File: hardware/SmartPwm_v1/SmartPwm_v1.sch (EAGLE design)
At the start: 41 parts, among them IC1 7805T, J1 ESP32-PICO-KIT, Q1 IRF3704-H, Q2 IRF3704-H, Q3 IRF3704-H, Q4 IRF3704-H, U1 ICL7667CBAZA, U3 ICL7667CBAZA

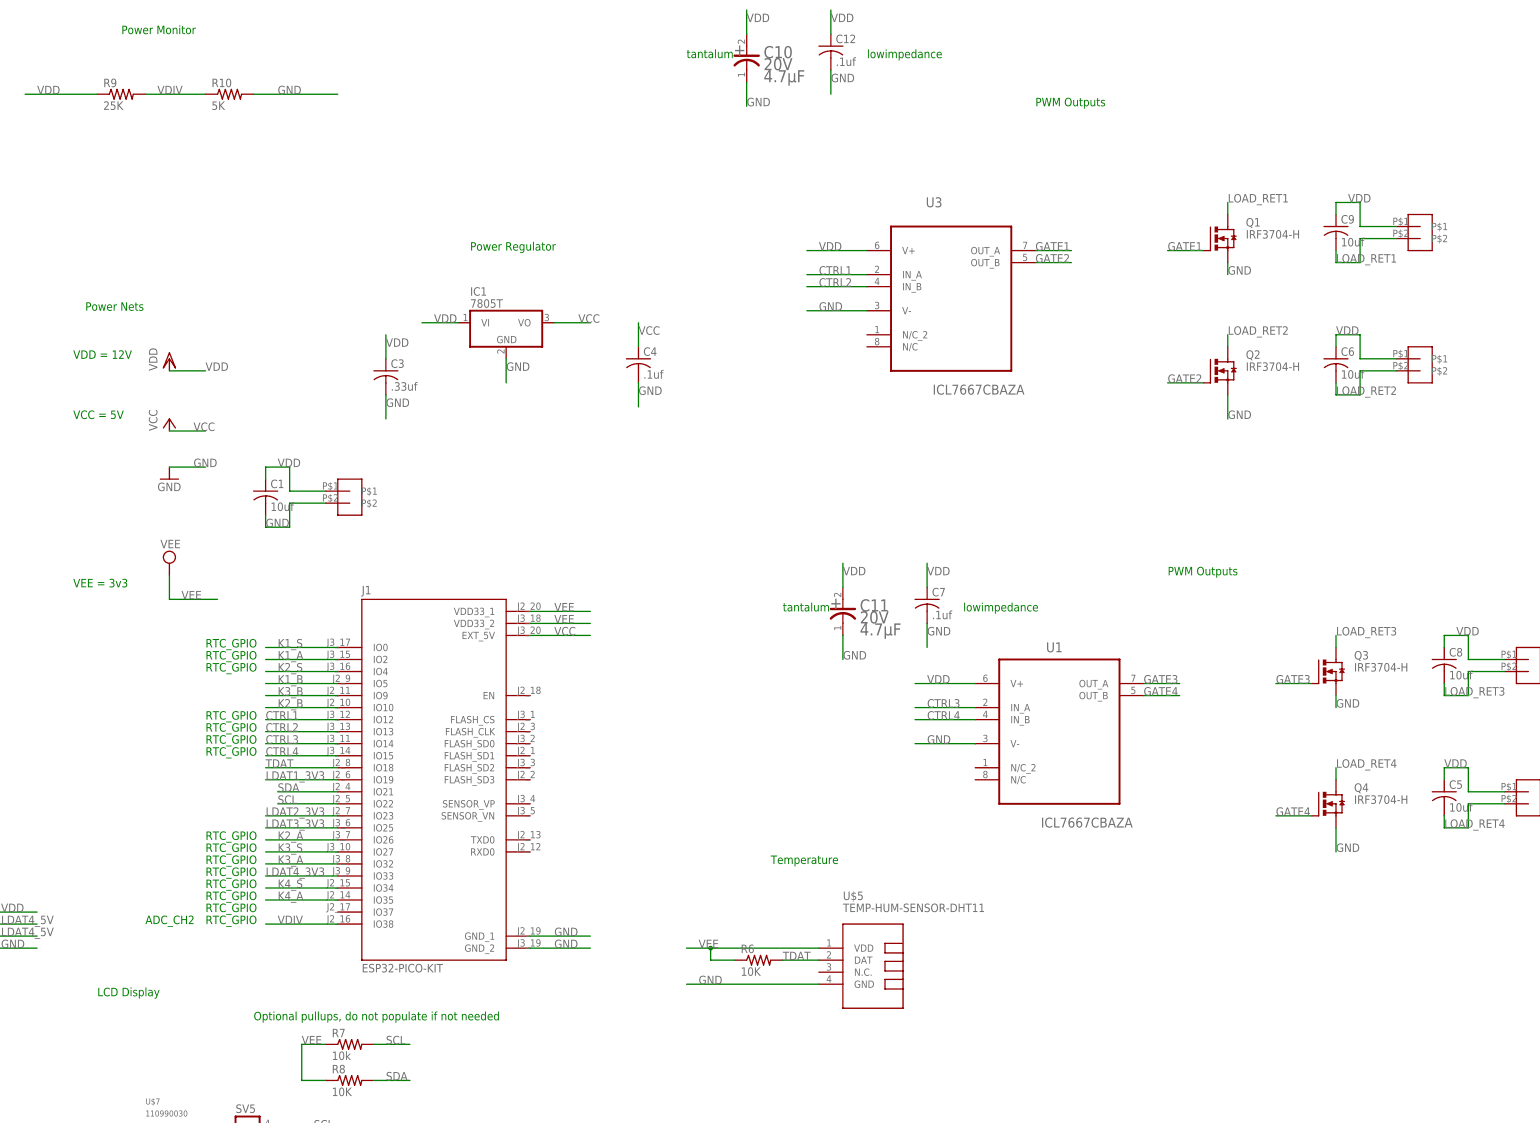
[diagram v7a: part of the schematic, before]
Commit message: redo placment for more efficient routing
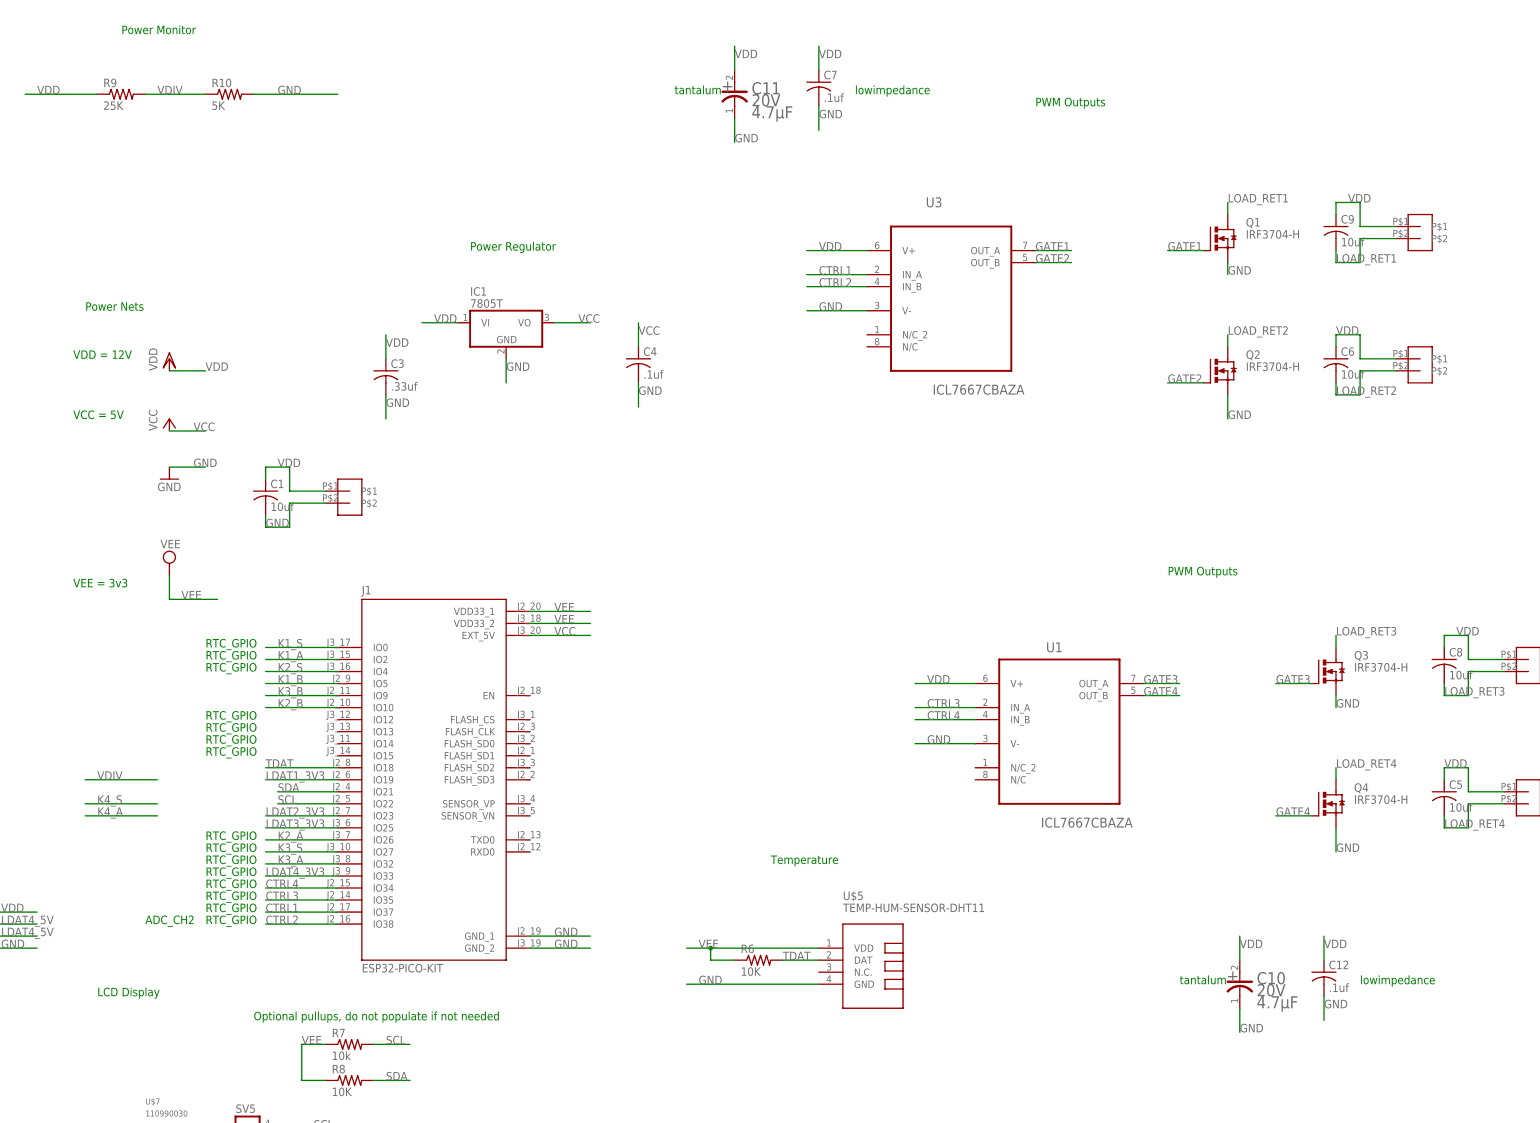
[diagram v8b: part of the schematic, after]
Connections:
- net CTRL1: now also J1.IO37; no longer J1.IO12
- net CTRL2: now also J1.IO38; no longer J1.IO13
- net CTRL3: now also J1.IO35; no longer J1.IO14
- net CTRL4: now also J1.IO34; no longer J1.IO15
- net K4_A: no longer J1.IO35
- net K4_S: no longer J1.IO34
- net VDIV: no longer J1.IO38
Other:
- moved on the sheet: C10, C11, C12, C7
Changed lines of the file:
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@@
 <text x="5.08" y="142.24" size="1.778" layer="91">Power Monitor</text>
 <text x="-5.08" y="25.4" size="1.778" layer="91">VEE = 3v3</text>
-<text x="144.78" y="20.32" size="1.778" layer="91">tantalum</text>
-<text x="182.88" y="20.32" size="1.778" layer="91">lowimpedance</text>
+<text x="121.92" y="129.54" size="1.778" layer="91">tantalum</text>
+<text x="160.02" y="129.54" size="1.778" layer="91">lowimpedance</text>
 <text x="33.02" y="-66.04" size="1.778" layer="91">Optional pullups, do not populate if not needed</text>
 <text x="-15.24" y="-109.22" size="1.778" layer="91">Optional, connector if desired to go grove to grove. beware of orintation during install</text>
-<text x="124.46" y="137.16" size="1.778" layer="91">tantalum</text>
-<text x="162.56" y="137.16" size="1.778" layer="91">lowimpedance</text>
+<text x="228.6" y="-58.42" size="1.778" layer="91">tantalum</text>
+<text x="266.7" y="-58.42" size="1.778" layer="91">lowimpedance</text>
 </plain>
 <instances>
@@
 <attribute name="VALUE" x="10.16" y="-86.36" size="1.27" layer="96"/>
 </instance>
-<instance part="C11" gate="G$0" x="154.94" y="22.86" smashed="yes">
-<attribute name="NAME" x="161.036" y="22.86" size="2.54" layer="95" align="top-left"/>
-</instance>
-<instance part="C7" gate="G$1" x="175.26" y="22.86" smashed="yes">
-<attribute name="NAME" x="176.276" y="23.495" size="1.778" layer="95"/>
-<attribute name="VALUE" x="176.276" y="18.669" size="1.778" layer="96"/>
+<instance part="C11" gate="G$0" x="132.08" y="132.08" smashed="yes">
+<attribute name="NAME" x="138.176" y="132.08" size="2.54" layer="95" align="top-left"/>
+</instance>
+<instance part="C7" gate="G$1" x="152.4" y="132.08" smashed="yes">
+<attribute name="NAME" x="153.416" y="132.715" size="1.778" layer="95"/>
+<attribute name="VALUE" x="153.416" y="127.889" size="1.778" layer="96"/>
 </instance>
 <instance part="C8" gate="G$1" x="284.48" y="10.16" smashed="yes">
@@
 <attribute name="VALUE" x="262.636" y="97.409" size="1.778" layer="96"/>
 </instance>
-<instance part="C10" gate="G$0" x="134.62" y="139.7" smashed="yes">
-<attribute name="NAME" x="140.716" y="139.7" size="2.54" layer="95" align="top-left"/>
-</instance>
-<instance part="C12" gate="G$1" x="154.94" y="139.7" smashed="yes">
-<attribute name="NAME" x="155.956" y="140.335" size="1.778" layer="95"/>
-<attribute name="VALUE" x="155.956" y="135.509" size="1.778" layer="96"/>
+<instance part="C10" gate="G$0" x="238.76" y="-55.88" smashed="yes">
+<attribute name="NAME" x="244.856" y="-55.88" size="2.54" layer="95" align="top-left"/>
+</instance>
+<instance part="C12" gate="G$1" x="259.08" y="-55.88" smashed="yes">
+<attribute name="NAME" x="260.096" y="-55.245" size="1.778" layer="95"/>
+<attribute name="VALUE" x="260.096" y="-60.071" size="1.778" layer="96"/>
 </instance>
 <instance part="C3" gate="G$1" x="60.96" y="71.12" smashed="yes">
@@
 </segment>
 <segment>
-<label x="157.48" y="10.16" size="1.778" layer="95"/>
+<label x="134.62" y="119.38" size="1.778" layer="95"/>
 <pinref part="C11" gate="G$0" pin="CATHODE"/>
-<wire x1="157.48" y1="15.24" x2="157.48" y2="10.16" width="0.1524" layer="91"/>
-</segment>
-<segment>
-<wire x1="175.26" y1="17.78" x2="175.26" y2="12.7" width="0.1524" layer="91"/>
-<label x="175.26" y="15.24" size="1.778" layer="95"/>
+<wire x1="134.62" y1="124.46" x2="134.62" y2="119.38" width="0.1524" layer="91"/>
+</segment>
+<segment>
+<wire x1="152.4" y1="127" x2="152.4" y2="121.92" width="0.1524" layer="91"/>
+<label x="152.4" y="124.46" size="1.778" layer="95"/>
 <pinref part="C7" gate="G$1" pin="2"/>
 </segment>
@@
 </segment>
 <segment>
-<label x="137.16" y="127" size="1.778" layer="95"/>
+<label x="241.3" y="-68.58" size="1.778" layer="95"/>
 <pinref part="C10" gate="G$0" pin="CATHODE"/>
-<wire x1="137.16" y1="132.08" x2="137.16" y2="127" width="0.1524" layer="91"/>
-</segment>
-<segment>
-<wire x1="154.94" y1="134.62" x2="154.94" y2="129.54" width="0.1524" layer="91"/>
-<label x="154.94" y="132.08" size="1.778" layer="95"/>
+<wire x1="241.3" y1="-63.5" x2="241.3" y2="-68.58" width="0.1524" layer="91"/>
+</segment>
+<segment>
+<wire x1="259.08" y1="-60.96" x2="259.08" y2="-66.04" width="0.1524" layer="91"/>
+<label x="259.08" y="-63.5" size="1.778" layer="95"/>
 <pinref part="C12" gate="G$1" pin="2"/>
 </segment>
@@
 </segment>
 <segment>
-<wire x1="157.48" y1="25.4" x2="157.48" y2="30.48" width="0.1524" layer="91"/>
-<label x="157.48" y="27.94" size="1.778" layer="95"/>
+<wire x1="134.62" y1="134.62" x2="134.62" y2="139.7" width="0.1524" layer="91"/>
+<label x="134.62" y="137.16" size="1.778" layer="95"/>
 <pinref part="C11" gate="G$0" pin="ANODE"/>
 </segment>
 <segment>
-<wire x1="175.26" y1="25.4" x2="175.26" y2="30.48" width="0.1524" layer="91"/>
-<label x="175.26" y="27.94" size="1.778" layer="95"/>
+<wire x1="152.4" y1="134.62" x2="152.4" y2="139.7" width="0.1524" layer="91"/>
+<label x="152.4" y="137.16" size="1.778" layer="95"/>
 <pinref part="C7" gate="G$1" pin="1"/>
 </segment>
@@
 </segment>
 <segment>
-<wire x1="137.16" y1="142.24" x2="137.16" y2="147.32" width="0.1524" layer="91"/>
-<label x="137.16" y="144.78" size="1.778" layer="95"/>
+<wire x1="241.3" y1="-53.34" x2="241.3" y2="-48.26" width="0.1524" layer="91"/>
+<label x="241.3" y="-50.8" size="1.778" layer="95"/>
 <pinref part="C10" gate="G$0" pin="ANODE"/>
 </segment>
 <segment>
-<wire x1="154.94" y1="142.24" x2="154.94" y2="147.32" width="0.1524" layer="91"/>
-<label x="154.94" y="144.78" size="1.778" layer="95"/>
+<wire x1="259.08" y1="-53.34" x2="259.08" y2="-48.26" width="0.1524" layer="91"/>
+<label x="259.08" y="-50.8" size="1.778" layer="95"/>
 <pinref part="C12" gate="G$1" pin="1"/>
 </segment>
@@
 </segment>
 <segment>
-<wire x1="50.8" y1="-2.54" x2="35.56" y2="-2.54" width="0.1524" layer="91"/>
-<pinref part="J1" gate="G$1" pin="IO12"/>
-<label x="35.56" y="-2.54" size="1.778" layer="95"/>
+<wire x1="50.8" y1="-43.18" x2="35.56" y2="-43.18" width="0.1524" layer="91"/>
+<label x="35.56" y="-43.18" size="1.778" layer="95"/>
+<pinref part="J1" gate="G$1" pin="IO37"/>
 </segment>
 </net>
@@
 </segment>
 <segment>
-<wire x1="50.8" y1="-5.08" x2="35.56" y2="-5.08" width="0.1524" layer="91"/>
-<pinref part="J1" gate="G$1" pin="IO13"/>
-<label x="35.56" y="-5.08" size="1.778" layer="95"/>
+<wire x1="50.8" y1="-45.72" x2="35.56" y2="-45.72" width="0.1524" layer="91"/>
+<label x="35.56" y="-45.72" size="1.778" layer="95"/>
+<pinref part="J1" gate="G$1" pin="IO38"/>
 </segment>
 </net>
@@
 </segment>
 <segment>
-<wire x1="50.8" y1="-10.16" x2="35.56" y2="-10.16" width="0.1524" layer="91"/>
-<pinref part="J1" gate="G$1" pin="IO15"/>
-<label x="35.56" y="-10.16" size="1.778" layer="95"/>
+<wire x1="50.8" y1="-38.1" x2="35.56" y2="-38.1" width="0.1524" layer="91"/>
+<label x="35.56" y="-38.1" size="1.778" layer="95"/>
+<pinref part="J1" gate="G$1" pin="IO34"/>
 </segment>
 </net>
@@
 </segment>
 <segment>
-<wire x1="50.8" y1="-7.62" x2="35.56" y2="-7.62" width="0.1524" layer="91"/>
-<pinref part="J1" gate="G$1" pin="IO14"/>
-<label x="35.56" y="-7.62" size="1.778" layer="95"/>
+<wire x1="50.8" y1="-40.64" x2="35.56" y2="-40.64" width="0.1524" layer="91"/>
+<label x="35.56" y="-40.64" size="1.778" layer="95"/>
+<pinref part="J1" gate="G$1" pin="IO35"/>
 </segment>
 </net>
@@
 </segment>
 <segment>
-<wire x1="35.56" y1="-38.1" x2="50.8" y2="-38.1" width="0.1524" layer="91"/>
-<label x="38.1" y="-38.1" size="1.778" layer="95"/>
-<pinref part="J1" gate="G$1" pin="IO34"/>
+<wire x1="-2.54" y1="-20.32" x2="12.7" y2="-20.32" width="0.1524" layer="91"/>
+<label x="0" y="-20.32" size="1.778" layer="95"/>
 </segment>
 </net>
@@
 </segment>
 <segment>
-<wire x1="35.56" y1="-40.64" x2="50.8" y2="-40.64" width="0.1524" layer="91"/>
-<label x="38.1" y="-40.64" size="1.778" layer="95"/>
-<pinref part="J1" gate="G$1" pin="IO35"/>
+<wire x1="-2.54" y1="-22.86" x2="12.7" y2="-22.86" width="0.1524" layer="91"/>
+<label x="0" y="-22.86" size="1.778" layer="95"/>
 </segment>
 </net>
@@
 </net>
 <net name="VDIV" class="0">
-<segment>
-<pinref part="J1" gate="G$1" pin="IO38"/>
-<wire x1="50.8" y1="-45.72" x2="35.56" y2="-45.72" width="0.1524" layer="91"/>
-<label x="38.1" y="-45.72" size="1.778" layer="95"/>
-</segment>
 <segment>
 <wire x1="10.16" y1="129.54" x2="22.86" y2="129.54" width="0.1524" layer="91"/>
@@
 <pinref part="R10" gate="G$1" pin="1"/>
 </segment>
-</net>
+<segment>
+<wire x1="12.7" y1="-15.24" x2="-2.54" y2="-15.24" width="0.1524" layer="91"/>
+<label x="0" y="-15.24" size="1.778" layer="95"/>
+</segment>
+</net>
